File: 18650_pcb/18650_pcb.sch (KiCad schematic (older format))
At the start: 3 parts, among them P1 CONN_01X02

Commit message: Almost ready; needs cutouts for breakouts and positioning of connector
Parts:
- BT1: footprint footprints:KEYSTONE_1048_1049 -> footprints:KEYSTONE_1048
- P1: footprint Pin_Headers:Pin_Header_Straight_1x02_Pitch2.54mm -> Terminal_Blocks:TerminalBlock_Pheonix_PT-3.5mm_2pol
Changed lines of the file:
@@
 F 0 "BT1" H 4450 3750 50  0000 L CNN
 F 1 "2x_Battery_Holder" H 4400 3250 50  0000 L CNN
-F 2 "footprints:KEYSTONE_1048_1049" V 4800 3540 50  0001 C CNN
+F 2 "footprints:KEYSTONE_1048" V 4800 3540 50  0001 C CNN
 F 3 "" V 4800 3540 50  0000 C CNN
 	1    4700 3500
@@
 F 0 "P1" H 4000 3650 50  0000 C CNN
 F 1 "CONN_01X02" V 4100 3500 50  0000 C CNN
-F 2 "Pin_Headers:Pin_Header_Straight_1x02_Pitch2.54mm" H 4000 3500 50  0001 C CNN
+F 2 "Terminal_Blocks:TerminalBlock_Pheonix_PT-3.5mm_2pol" H 4000 3500 50  0001 C CNN
 F 3 "" H 4000 3500 50  0000 C CNN
 	1    4000 3500

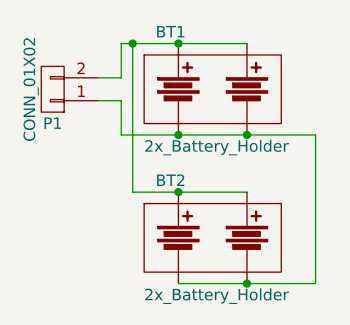
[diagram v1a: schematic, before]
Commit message: 18650 PCB modifications
-Added version information
-Added a fuse between two batteries
-Added polarity silkscreen markings
-Removed traces from bottom layer to prevent them from shorting out to
metal on back PCB
-Added pads for hand-soldering JST connector wires onto the board
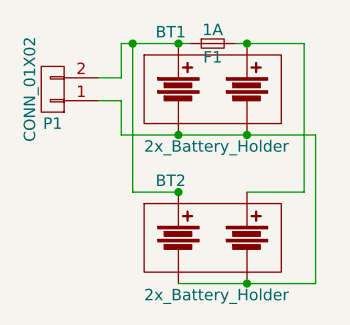
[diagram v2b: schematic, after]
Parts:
- added F1: 1A, Fuse_Holders_and_Fuses:Fuse_0679H, symbol Fuse_Small
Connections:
- net at BT1.1, BT2.1, P1.2 (P2): now also F1.1; no longer BT1.2, BT2.2
- new net: BT1.2, BT2.2, F1.2
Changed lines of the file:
@@
 $EndComp
-Wire Wire Line
-	4300 3300 4850 3300
 Wire Wire Line
 	4300 3700 5150 3700
@@
 Connection ~ 4550 3300
 Wire Wire Line
-	4350 3950 4850 3950
-Wire Wire Line
 	4550 4350 5150 4350
 Wire Wire Line
@@
 Connection ~ 4550 3950
 Connection ~ 4350 3300
+Wire Wire Line
+	4300 3300 4600 3300
+$Comp
+L Fuse_Small F1
+U 1 1 59A89BD5
+P 4700 3300
+F 0 "F1" H 4700 3240 50  0000 C CNN
+F 1 "1A" H 4700 3360 50  0000 C CNN
+F 2 "Fuse_Holders_and_Fuses:Fuse_0679H" H 4700 3300 50  0001 C CNN
+F 3 "" H 4700 3300 50  0001 C CNN
+	1    4700 3300
+	1    0    0    -1
+$EndComp
+Wire Wire Line
+	4800 3300 5100 3300
+Wire Wire Line
+	4350 3950 4550 3950
+Wire Wire Line
+	4850 3950 5100 3950
+Wire Wire Line
+	5100 3950 5100 3300
+Connection ~ 4850 3300
 $EndSCHEMATC

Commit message: Started KiCad 5 migration
Opened each schematic, "rescued" symbols, then saved the files. No .kicad_pcb file changes so far.
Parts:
- BT1, BT2: symbol 2X_Battery_Holder -> battery_holder:2X_Battery_Holder
- F1: symbol Fuse_Small -> 18650_pcb-rescue:Fuse_Small
- P1: symbol CONN_01X02 -> 18650_pcb-rescue:CONN_01X02
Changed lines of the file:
@@
-EESchema Schematic File Version 2
-LIBS:18650_pcb-rescue
-LIBS:power
-LIBS:device
-LIBS:transistors
-LIBS:conn
-LIBS:linear
-LIBS:regul
-LIBS:74xx
-LIBS:cmos4000
-LIBS:adc-dac
-LIBS:memory
-LIBS:xilinx
-LIBS:microcontrollers
-LIBS:dsp
-LIBS:microchip
-LIBS:analog_switches
-LIBS:motorola
-LIBS:texas
-LIBS:intel
-LIBS:audio
-LIBS:interface
-LIBS:digital-audio
-LIBS:philips
-LIBS:display
-LIBS:cypress
-LIBS:siliconi
-LIBS:opto
-LIBS:atmel
-LIBS:contrib
-LIBS:valves
-LIBS:battery_holder
+EESchema Schematic File Version 4
 LIBS:18650_pcb-cache
-EELAYER 25 0
+EELAYER 26 0
 EELAYER END
 $Descr A4 11693 8268
@@
 $EndDescr
 $Comp
-L 2X_Battery_Holder BT1
+L battery_holder:2X_Battery_Holder BT1
 U 1 1 590D1921
 P 4700 3500
@@
 $EndComp
 $Comp
-L CONN_01X02 P1
+L 18650_pcb-rescue:CONN_01X02 P1
 U 1 1 590D1D4A
 P 4000 3500
@@
 $EndComp
 $Comp
-L 2X_Battery_Holder BT2
+L battery_holder:2X_Battery_Holder BT2
 U 1 1 590D1DD3
 P 4700 4150
@@
 $EndComp
 Wire Wire Line
-	4300 3700 5150 3700
+	4300 3700 4550 3700
 Wire Wire Line
 	4300 3700 4300 3550
@@
 Connection ~ 4550 3300
 Wire Wire Line
-	4550 4350 5150 4350
+	4550 4350 4850 4350
 Wire Wire Line
 	5150 4350 5150 3700
@@
 Wire Wire Line
 	4350 3300 4350 3950
-Connection ~ 4550 3950
 Connection ~ 4350 3300
 Wire Wire Line
-	4300 3300 4600 3300
+	4300 3300 4350 3300
 $Comp
-L Fuse_Small F1
+L 18650_pcb-rescue:Fuse_Small F1
 U 1 1 59A89BD5
 P 4700 3300
@@
 $EndComp
 Wire Wire Line
-	4800 3300 5100 3300
+	4800 3300 4850 3300
 Wire Wire Line
 	4350 3950 4550 3950
@@
 	5100 3950 5100 3300
 Connection ~ 4850 3300
+Wire Wire Line
+	4550 3700 4850 3700
+Wire Wire Line
+	4550 3300 4600 3300
+Wire Wire Line
+	4850 3700 5150 3700
+Wire Wire Line
+	4850 4350 5150 4350
+Wire Wire Line
+	4350 3300 4550 3300
+Wire Wire Line
+	4850 3300 5100 3300
 $EndSCHEMATC
